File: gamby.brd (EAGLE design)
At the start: 53.3 x 69.2 mm, 61 parts, among them Q1 2N3704

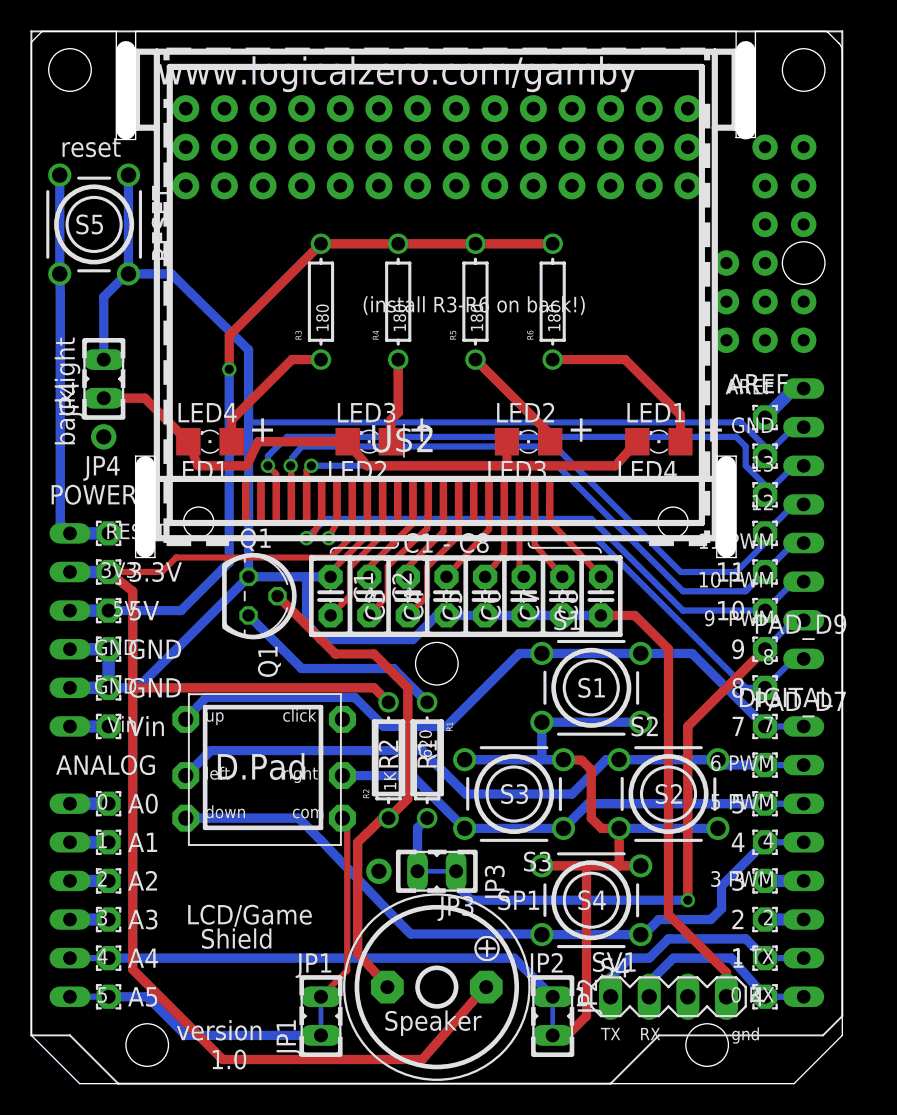
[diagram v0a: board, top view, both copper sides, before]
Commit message: Moved and added generic pads, enlarged holes over Uno R3 SCL/SDA pins, increased clearances.
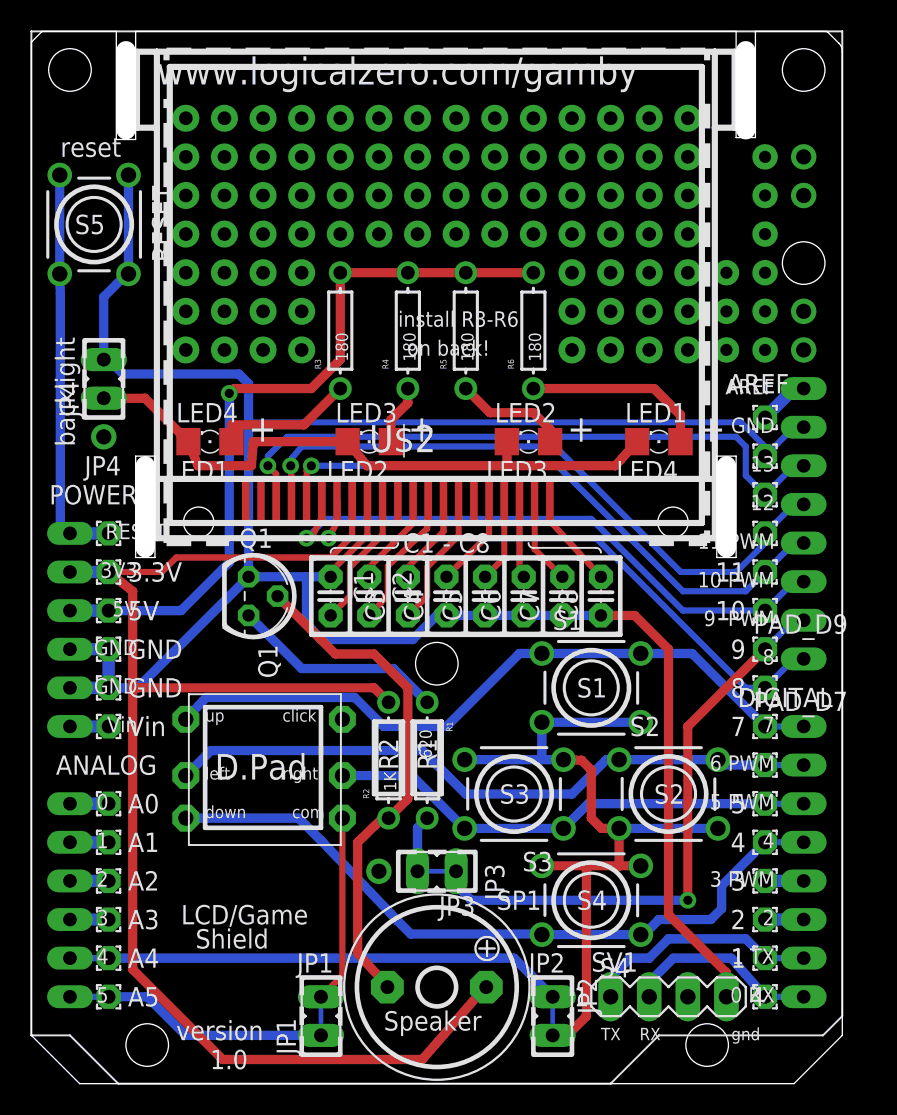
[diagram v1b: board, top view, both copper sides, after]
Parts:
- moved R3 2.29 mm to (20.3, 48.9)
- moved R6 2.29 mm to (33.0, 48.9)
- moved R4 2.01 mm to (24.8, 48.9)
- moved R5 2.01 mm to (28.6, 48.9)
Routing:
- net GND: track 161.3 -> 159.3 mm
- net N$7: track 5.77 -> 4.13 mm
- net +5V: track 50.5 -> 49.5 mm
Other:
- board text added: "install R3-R6"
- board text added: "on back!"
- board text removed: "(install R3-R6 on back!)"

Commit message: Minor tweaks, mostly cosmetic; added board images with part placement.
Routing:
- net N$4: track 42.4 -> 45.5 mm
- net N$3: track 39.5 -> 41.9 mm
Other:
- board text added: "(cc) 2012 D.R. Stokes"
- board text removed: "1"
- board text removed: "10"
- board text removed: "11"
- board text removed: "2"
- board text removed: "3"
- board text removed: "3.3V"
- board text removed: "4"
- board text removed: "5"
- board text removed: "5V"
- board text removed: "7"
- board text removed: "8"
- board text removed: "9"
- board text removed: "A0"
- board text removed: "A1"
- board text removed: "A2"
- board text removed: "A3"
- board text removed: "A4"
- board text removed: "A5"
- board text removed: "AREF"
- board text removed: "GND"
- board text removed: "Vin"
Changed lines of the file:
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@@
 <circle x="26.67" y="5.715" radius="5.2555" width="0.3048" layer="121"/>
 <circle x="26.67" y="5.715" radius="1.27" width="0.3048" layer="121"/>
-<text x="9.525" y="2.2225" size="1.27" layer="121" font="vector" ratio="15">version</text>
-<text x="46.99" y="10.795" size="1.27" layer="121" font="vector" rot="R180">2</text>
+<text x="9.2075" y="4.7625" size="1.27" layer="121" font="vector" ratio="15">version</text>
 <text x="12.065" y="19.3675" size="1.6764" layer="121" font="vector">D.Pad</text>
 <text x="35.8775" y="24.765" size="1.27" layer="121" font="vector">S1</text>
@@
 <text x="20.0025" y="42.8625" size="1.27" layer="121" font="vector">LED3</text>
 <text x="9.525" y="42.8625" size="1.27" layer="121" font="vector">LED4</text>
-<text x="8.89" y="11.43" size="2.54" layer="29" font="vector" ratio="20">Gamby</text>
-<text x="11.7475" y="0.3175" size="1.27" layer="121" font="vector" ratio="15">1.0</text>
-<text x="9.8425" y="9.8425" size="1.27" layer="121" font="vector" ratio="20">LCD/Game</text>
-<text x="10.795" y="8.255" size="1.27" layer="121" font="vector" ratio="20">Shield</text>
-<text x="6.35" y="12.065" size="1.27" layer="121" font="vector">A2</text>
-<text x="6.35" y="14.605" size="1.27" layer="121" font="vector">A1</text>
-<text x="6.35" y="17.145" size="1.27" layer="121" font="vector">A0</text>
-<text x="6.35" y="24.765" size="1.27" layer="121" font="vector">GND</text>
-<text x="6.35" y="27.305" size="1.27" layer="121" font="vector">GND</text>
-<text x="6.35" y="29.845" size="1.27" layer="121" font="vector">5V</text>
-<text x="6.35" y="32.385" size="1.27" layer="121" font="vector">3.3V</text>
-<text x="6.35" y="9.525" size="1.27" layer="121" font="vector">A3</text>
-<text x="6.35" y="6.985" size="1.27" layer="121" font="vector">A4</text>
-<text x="6.35" y="4.445" size="1.27" layer="121" font="vector">A5</text>
-<text x="6.35" y="22.225" size="1.27" layer="121" font="vector">Vin</text>
+<text x="7.3025" y="11.43" size="2.8575" layer="29" font="vector" ratio="20">Gamby</text>
+<text x="11.7475" y="2.8575" size="1.27" layer="121" font="vector" ratio="15">1.0</text>
+<text x="8.5725" y="9.8425" size="1.27" layer="121" font="vector" ratio="20">LCD/Game</text>
+<text x="9.8425" y="8.255" size="1.27" layer="121" font="vector" ratio="20">Shield</text>
 <text x="3.4925" y="39.37" size="1.27" layer="121" font="vector">JP4</text>
 <text x="24.4475" y="34.29" size="1.27" layer="121" font="vector">C1 - C8</text>
-<text x="19.685" y="47.9425" size="1.27" layer="29" font="vector" rot="MR90">R3</text>
-<text x="46.99" y="13.335" size="1.27" layer="121" font="vector" rot="R180">3</text>
-<text x="46.99" y="15.875" size="1.27" layer="121" font="vector" rot="R180">4</text>
-<text x="46.99" y="18.415" size="1.27" layer="121" font="vector" rot="R180">5</text>
-<text x="46.99" y="23.495" size="1.27" layer="121" font="vector" rot="R180">7</text>
-<text x="46.99" y="26.035" size="1.27" layer="121" font="vector" rot="R180">8</text>
-<text x="46.99" y="28.575" size="1.27" layer="121" font="vector" rot="R180">9</text>
-<text x="46.99" y="31.115" size="1.27" layer="121" font="vector" rot="R180">10</text>
-<text x="46.99" y="33.655" size="1.27" layer="121" font="vector" rot="R180">11</text>
+<text x="19.685" y="47.9425" size="1.27" layer="30" font="vector" rot="MR90">R3</text>
 <text x="8.255" y="65.0875" size="1.778" layer="121" font="vector">www.logicalzero.com/gamby</text>
-<text x="37.465" y="2.2225" size="0.8128" layer="121" font="vector">TX</text>
-<text x="40.005" y="2.2225" size="0.8128" layer="121" font="vector">RX</text>
-<text x="46.0375" y="2.2225" size="0.8128" layer="121" font="vector">gnd</text>
-<text x="49.8475" y="46.0375" size="1.27" layer="121" font="vector" rot="R180">AREF</text>
-<text x="46.99" y="8.255" size="1.27" layer="121" font="vector" rot="R180">1</text>
+<text x="37.465" y="6.985" size="0.8128" layer="121" font="vector">TX</text>
+<text x="40.005" y="6.985" size="0.8128" layer="121" font="vector">RX</text>
+<text x="44.45" y="6.985" size="0.8128" layer="121" font="vector">gnd</text>
 <text x="45.085" y="65.0875" size="1.778" layer="30" font="vector" ratio="15" rot="MR0">www.logicalzero.com/gamby</text>
-<text x="24.13" y="47.9425" size="1.27" layer="29" font="vector" rot="MR90">R4</text>
-<text x="27.94" y="47.9425" size="1.27" layer="29" font="vector" rot="MR90">R5</text>
-<text x="32.385" y="47.9425" size="1.27" layer="29" font="vector" rot="MR90">R6</text>
+<text x="24.13" y="47.9425" size="1.27" layer="30" font="vector" rot="MR90">R4</text>
+<text x="27.94" y="47.9425" size="1.27" layer="30" font="vector" rot="MR90">R5</text>
+<text x="32.385" y="47.9425" size="1.27" layer="30" font="vector" rot="MR90">R6</text>
 <text x="2.8575" y="41.275" size="1.27" layer="121" font="vector" rot="R90">backlight</text>
 <text x="32.0675" y="50.165" size="1.016" layer="121" font="vector" rot="R180">install R3-R6</text>
@@
 <hole x="50.8" y="66.04" drill="2.8"/>
 <text x="30.1625" y="48.26" size="1.016" layer="121" font="vector" rot="R180">on back!</text>
+<text x="7.2771" y="11.43" size="2.8575" layer="30" font="vector" ratio="25">Gamby</text>
+<text x="38.1" y="37.7825" size="1.27" layer="30" font="vector" ratio="15" rot="MR0">(cc) 2012 D.R. Stokes</text>
 </plain>
 <attributes>
@@
 <wire x1="46.99" y1="31.75" x2="48.26" y2="33.02" width="0.4064" layer="16"/>
 <wire x1="42.8625" y1="31.75" x2="46.99" y2="31.75" width="0.4064" layer="16"/>
-<wire x1="34.6075" y1="40.005" x2="42.8625" y2="31.75" width="0.4064" layer="16"/>
-<wire x1="18.415" y1="40.005" x2="34.6075" y2="40.005" width="0.4064" layer="16"/>
+<wire x1="38.735" y1="40.005" x2="38.735" y2="35.8775" width="0.4064" layer="16"/>
+<wire x1="38.735" y1="35.8775" x2="42.8625" y2="31.75" width="0.4064" layer="16"/>
+<wire x1="18.415" y1="40.005" x2="38.735" y2="40.005" width="0.4064" layer="16"/>
 <wire x1="18.105" y1="37.7425" x2="18.0975" y2="37.75" width="0.4064" layer="1"/>
 <wire x1="18.105" y1="39.695" x2="18.415" y2="40.005" width="0.4064" layer="1"/>
@@
 <wire x1="17.105" y1="39.3225" x2="17.0575" y2="40.005" width="0.4064" layer="1"/>
 <wire x1="17.105" y1="37.7425" x2="17.105" y2="39.3225" width="0.4064" layer="1"/>
-<wire x1="34.4576" y1="41.275" x2="42.7126" y2="33.02" width="0.4064" layer="16"/>
+<wire x1="34.4576" y1="41.275" x2="39.6875" y2="41.275" width="0.4064" layer="16"/>
+<wire x1="39.6875" y1="41.275" x2="39.6875" y2="35.8775" width="0.4064" layer="16"/>
+<wire x1="39.6875" y1="35.8775" x2="42.7126" y2="33.02" width="0.4064" layer="16"/>
 <wire x1="42.7126" y1="33.02" x2="46.355" y2="33.02" width="0.4064" layer="16"/>
 <wire x1="46.355" y1="33.02" x2="48.26" y2="34.925" width="0.4064" layer="16"/>

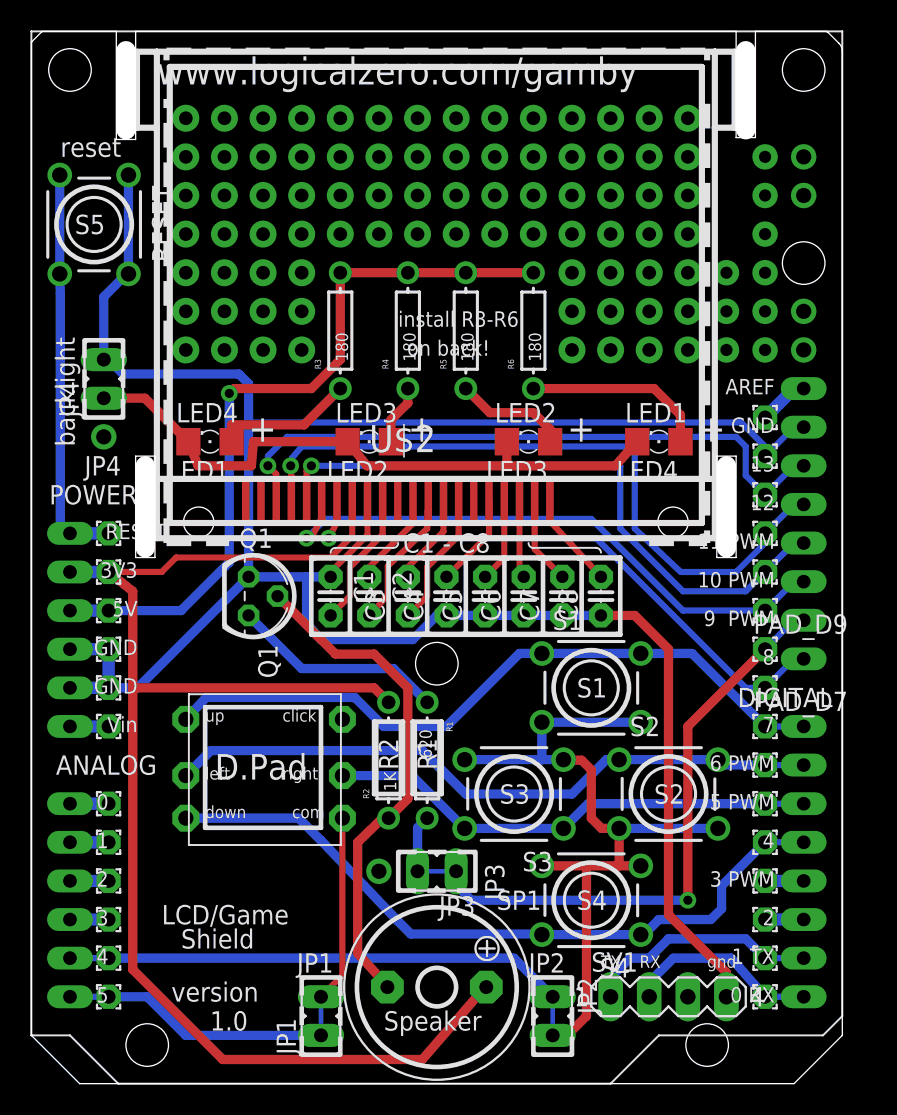
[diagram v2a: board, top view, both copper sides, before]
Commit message: Shifted secondary pads on 12, 13, AREF to improve clearance; added gerbers.
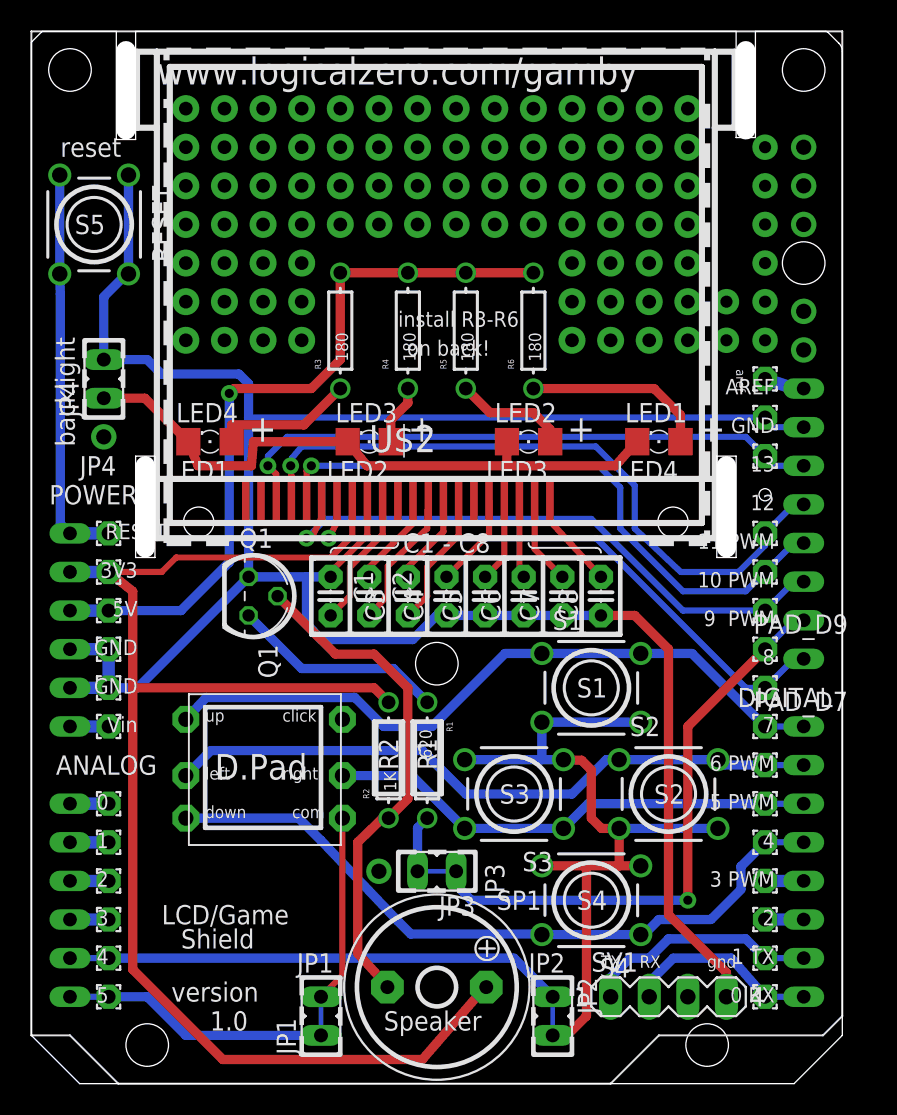
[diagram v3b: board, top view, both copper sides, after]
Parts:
- moved PAD_AREF 2.54 mm to (48.3, 45.7)
- moved PAD_D13 2.54 mm to (48.3, 40.6)
- moved PAD_GND0 2.54 mm to (48.3, 43.2)
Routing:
- net N$25: track 42.4 -> 39.7 mm
- net GND: track 159.3 -> 157.5 mm
- net N$4: track 45.5 -> 44.1 mm
- net N$3: track 41.9 -> 41.1 mm
- net N$49: track 3.33 -> 2.64 mm
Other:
- board text added: "aref"
